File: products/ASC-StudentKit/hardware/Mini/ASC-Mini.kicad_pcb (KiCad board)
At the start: 2 copper layers, 97.4 x 47 mm, 92 parts, among them J1 12V IN, J10 OUT2, J2 USB-C, J3 PROG, J4 S1, J5 S2, J6 S3, J7 S4, J8 I2C-1 (Grove), J9 OUT1, K1 HF46F/005-HS1, K2 HF46F/005-HS1, Q1 AO3400A, Q2 AO3400A, Q3 AO3400A, SW1 RESET, SW2 PAIR / BOOT, U1 ESP32-S3-MINI-1-N8, U2 TPS54202DDC, U3 USBLC6-2SC6, U4 AP7361C-33E, U5 DS3231MZ+

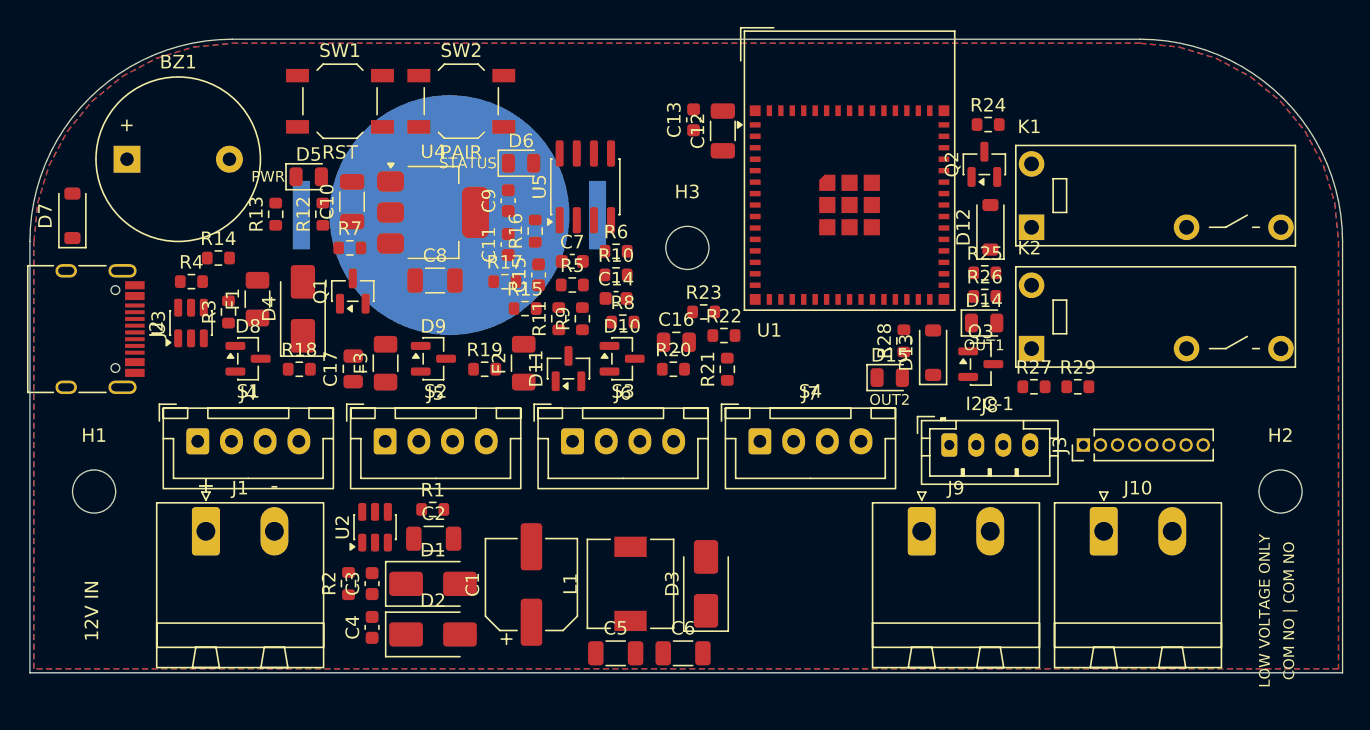
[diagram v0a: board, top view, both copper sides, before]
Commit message: Mini PCB: first Freerouting pass (partial: 19 connections open)
Freerouting 2.5.0, 18 passes, 0 violations: 1236 track segments and 112
vias. Still open: 44 GND connections (for the pours) and 14 on VIN,
VBUS_F, +3V3, +5V, EN, LED, LED_STATUS_A, RTC_INT and VIN_SENSE. The
placement gets loosened next.

Co-Authored-By: Claude Opus 5.5 <noreply@anthropic.com>
Claude-Session: https://claude.ai/code/session_0137TCDSR58nWZn1byy7MgSb
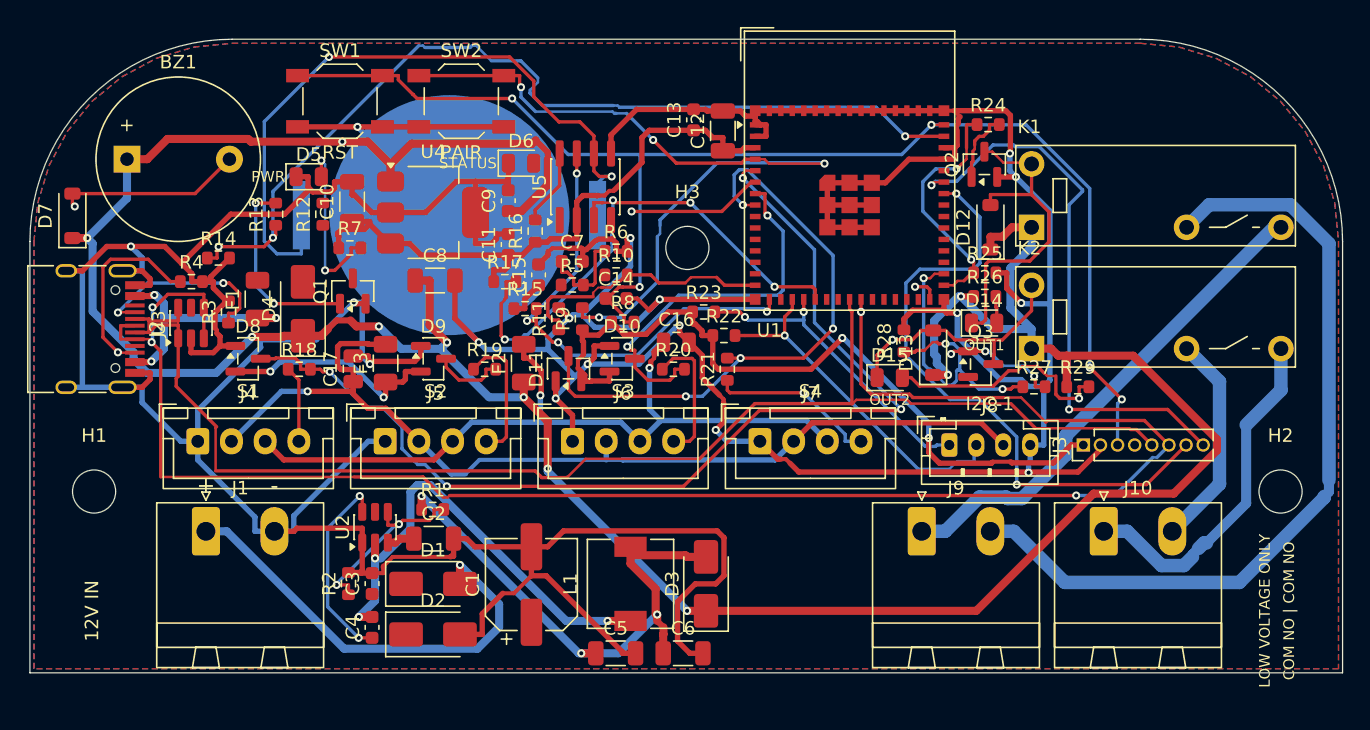
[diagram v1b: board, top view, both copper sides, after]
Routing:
- net GND: track 0.00 -> 492.9 mm, vias 0 -> 17
- net +5V: track 0.00 -> 215.9 mm, vias 0 -> 10
- net /USB_DP: track 0.00 -> 132.9 mm, vias 0 -> 4
- net +3V3: track 0.00 -> 121.4 mm, vias 0 -> 4
- net /USB_DN: track 0.00 -> 102.1 mm
- net /EN: track 0.00 -> 101.0 mm, vias 0 -> 5
- net /S1: track 0.00 -> 78.4 mm, vias 0 -> 4
- net /+3V3_PORT: track 0.00 -> 73.1 mm, vias 0 -> 1
- net /BUZZER: track 0.00 -> 69.0 mm, vias 0 -> 3
- net /OUT1_NO: track 0.00 -> 60.4 mm
- net /PAIR: track 0.00 -> 59.9 mm, vias 0 -> 4
- net /+5V_PORT: track 0.00 -> 58.5 mm, vias 0 -> 2
- net /VBAT_RTC: track 0.00 -> 52.1 mm, vias 0 -> 2
- net /TXD0: track 0.00 -> 46.3 mm, vias 0 -> 2
- net /S4: track 0.00 -> 44.4 mm, vias 0 -> 4
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
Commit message: Mini PCB: GND left to the pours, routing fixes
route.py leaves GND out of the autorouter: after import, each front SMD
GND pad gets a short track to its own via into the back pour, and a 4 mm
grid of stitching vias ties the two pours together. Every via and track
is checked for clearance against all other copper, the board edge, the
screw bosses and the antenna keep-out. Second run: 2 nets left open
(from 19). Clearance rule 0.19 mm (the USB-C footprint's own pad gaps
are exactly 0.2 mm).

Placement: R5 (VIN sense top) sits by the buck so VIN stays local; the
buzzer gate parts sit on Q1's gate; LED labels go under their LEDs. U3's
VBUS reference pin moves to VBUS (before the fuse).

Board in this commit is unrouted; the next run's result follows.

Co-Authored-By: Claude Opus 5.5 <noreply@anthropic.com>
Claude-Session: https://claude.ai/code/session_0137TCDSR58nWZn1byy7MgSb
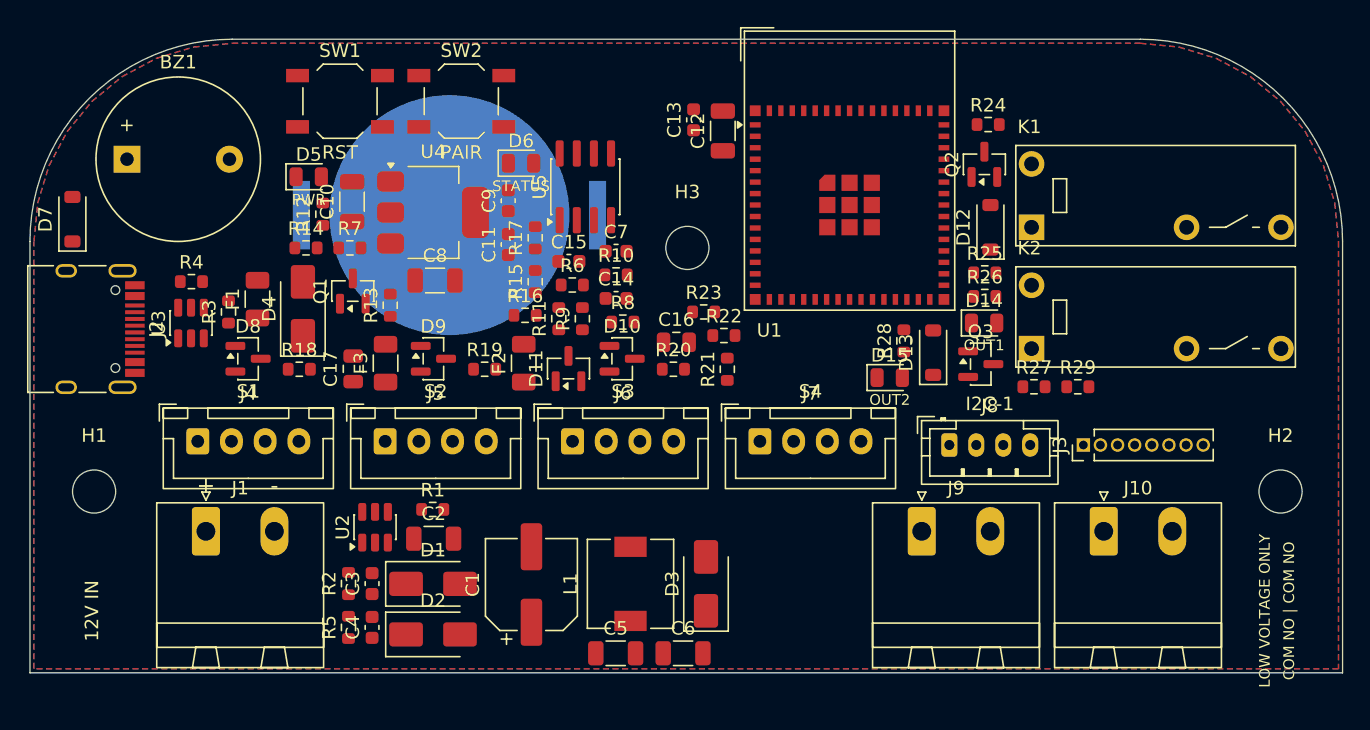
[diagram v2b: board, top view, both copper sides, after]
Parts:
- moved R5 30.3 mm to (123.6, 103.6), turned to 90 degrees
- moved R13 10.9 mm to (126.7, 79.7)
- moved R14 6.54 mm to (120.5, 75.5)
- moved R16 6.29 mm to (136.7, 80.5), turned to 0 degrees
- moved R6 4.10 mm to (140.2, 78.2)
- moved R17 3.95 mm to (137.5, 74.7), turned to 90 degrees
- moved C7 3.34 mm to (143.5, 75.7)
- moved C15 2.46 mm to (140.0, 76.5), turned to 0 degrees
- moved R15 2.14 mm to (137.5, 78.0), turned to 90 degrees
- moved D7 0.25 mm to (103.2, 73.3)
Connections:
- U3 pad 5: /VBUS_F -> /VBUS
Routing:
- net GND: track 492.9 -> 0.00 mm, vias 17 -> 0
- net +5V: track 215.9 -> 0.00 mm, vias 10 -> 0
- net /USB_DP: track 132.9 -> 0.00 mm, vias 4 -> 0
- net +3V3: track 121.4 -> 0.00 mm, vias 4 -> 0
- net /USB_DN: track 102.1 -> 0.00 mm
- net /EN: track 101.0 -> 0.00 mm, vias 5 -> 0
- net /S1: track 78.4 -> 0.00 mm, vias 4 -> 0
- net /+3V3_PORT: track 73.1 -> 0.00 mm, vias 1 -> 0
- net /BUZZER: track 69.0 -> 0.00 mm, vias 3 -> 0
- net /OUT1_NO: track 60.4 -> 0.00 mm
- net /PAIR: track 59.9 -> 0.00 mm, vias 4 -> 0
- net /+5V_PORT: track 58.5 -> 0.00 mm, vias 2 -> 0
- net /VBAT_RTC: track 52.1 -> 0.00 mm, vias 2 -> 0
- net /TXD0: track 46.3 -> 0.00 mm, vias 2 -> 0
- net /S4: track 44.4 -> 0.00 mm, vias 4 -> 0
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
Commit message: Mini PCB: all signals routed; pour check; GND routing stage
Variant b of three (power tracks 0.45 mm, supply 0.3 mm) routed every
signal connection (Freerouting 2.5.0, then its optimizer); its widths are
now the defaults. GND: pad vias, a 4 mm stitching grid, and island vias
from check_pour.py --fix.

tools/check_pour.py approximates KiCad's zone fill (0.1 mm raster, zone
clearance + half the minimum width) and checks every GND pad and via
lands in one connected GND. It still finds 16 pieces, where tracks on
both layers fence the pour in, so route.py gains a second stage
(ROUTE_STAGE=gnd): GND alone, routed as tracks around the protected
signal tracks.

Co-Authored-By: Claude Opus 5.5 <noreply@anthropic.com>
Claude-Session: https://claude.ai/code/session_0137TCDSR58nWZn1byy7MgSb
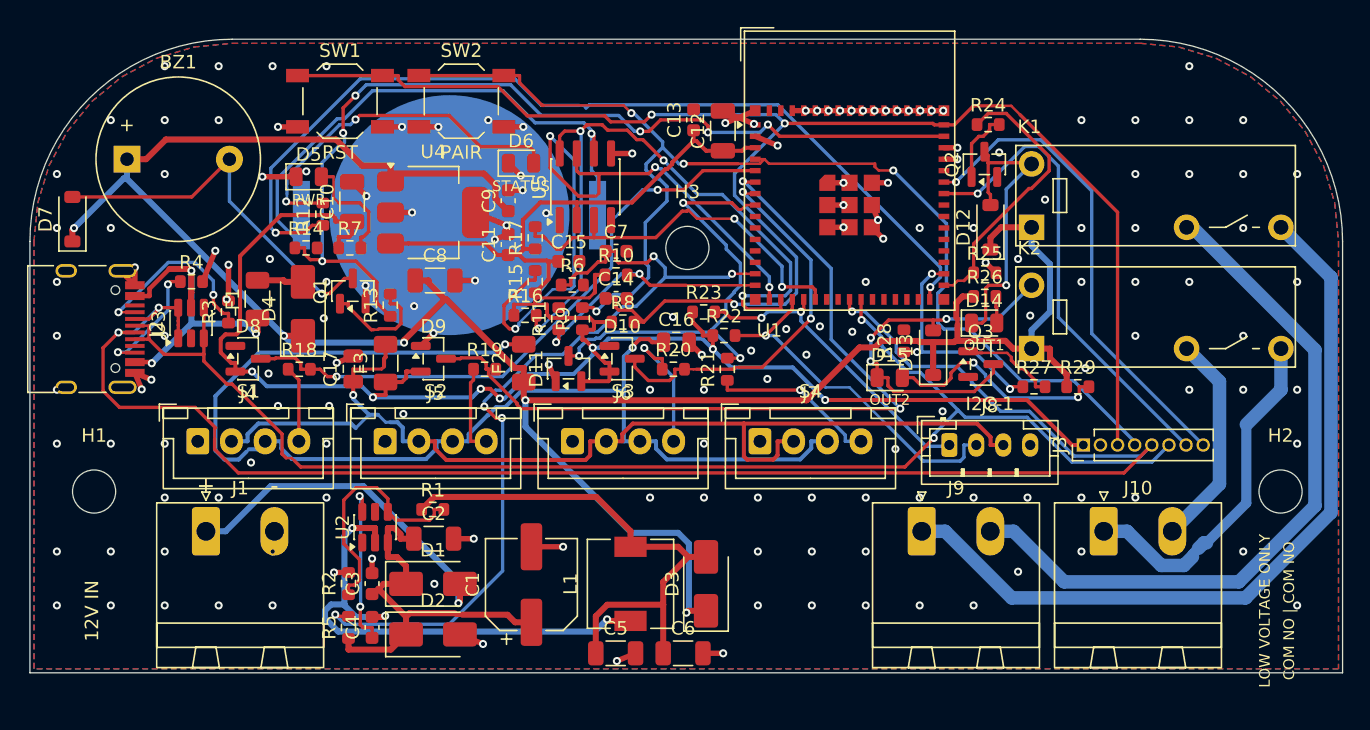
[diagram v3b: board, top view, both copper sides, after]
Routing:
- net +5V: track 0.00 -> 175.2 mm, vias 0 -> 5
- net +3V3: track 0.00 -> 168.3 mm, vias 0 -> 7
- net /USB_DN: track 0.00 -> 126.3 mm, vias 0 -> 3
- net /EN: track 0.00 -> 117.2 mm, vias 0 -> 3
- net /USB_DP: track 0.00 -> 103.2 mm, vias 0 -> 2
- net /+5V_PORT: track 0.00 -> 90.0 mm, vias 0 -> 2
- net /PAIR: track 0.00 -> 89.3 mm, vias 0 -> 4
- net /+3V3_PORT: track 0.00 -> 79.4 mm, vias 0 -> 1
- net GND: track 0.00 -> 78.4 mm, vias 0 -> 168
- net /BUZZER: track 0.00 -> 70.9 mm, vias 0 -> 6
- net /LED: track 0.00 -> 69.8 mm, vias 0 -> 2
- net /VIN_SENSE: track 0.00 -> 64.3 mm, vias 0 -> 5
- net /S2: track 0.00 -> 59.1 mm, vias 0 -> 2
- net /OUT1_COM: track 0.00 -> 57.7 mm
- net /I2C_INT_SDA: track 0.00 -> 53.1 mm, vias 0 -> 4
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
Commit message: Mini PCB: GND routing stage result (21 GND connections still open)
ROUTE_STAGE=gnd routed GND as tracks around the protected signals: 241
segments and 15 vias, 21 connections open; with the pours and 97
stitching vias, check_pour.py still finds 19 separate GND pieces. Two
layers at this density don't give a reliable GND.

Co-Authored-By: Claude Opus 5.5 <noreply@anthropic.com>
Claude-Session: https://claude.ai/code/session_0137TCDSR58nWZn1byy7MgSb
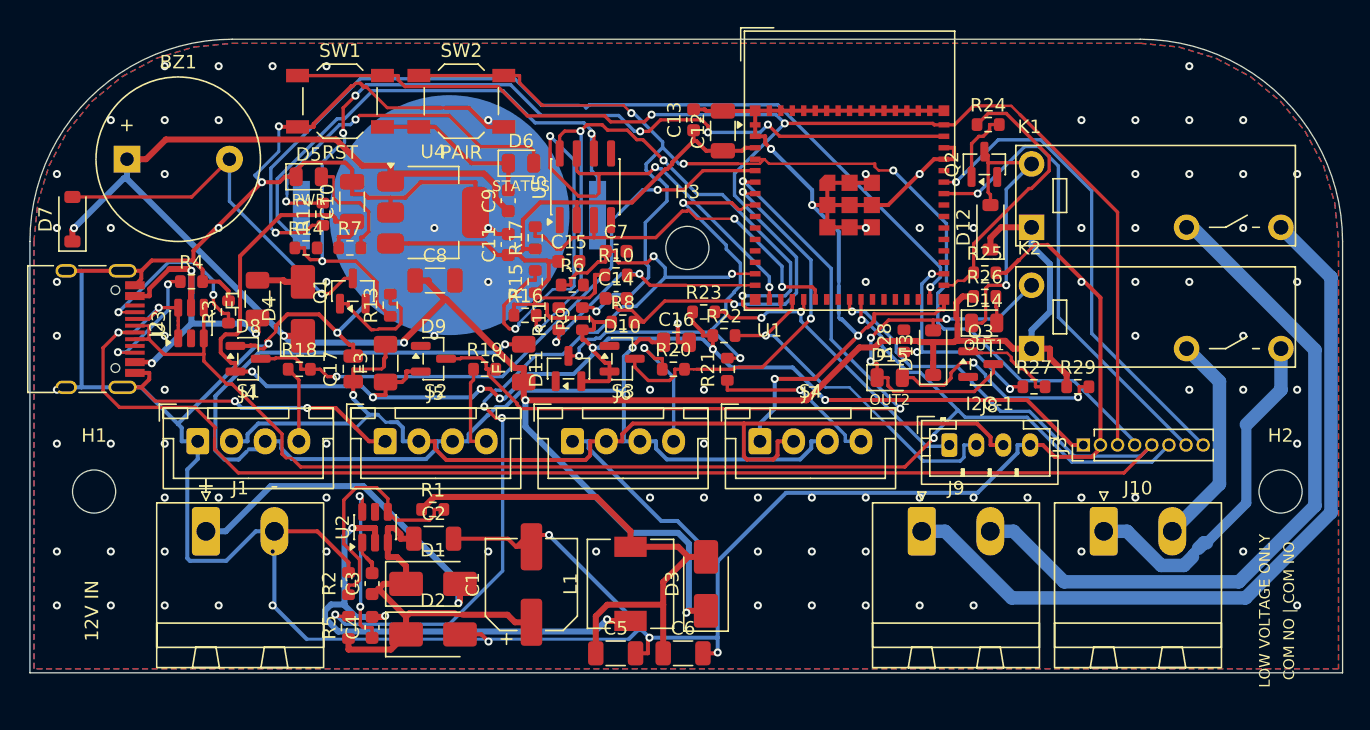
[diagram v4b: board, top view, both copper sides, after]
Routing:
- net GND: track 78.4 -> 417.6 mm, vias 168 -> 112

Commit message: Mini: 0402 passives, test header as pogo pads under the module
Staying on two layers frees routing room: the small resistors and
capacitors go from 0603 to 0402, and J3 (the tester's 8 pins) becomes an
SMD pad row on the back under the ESP32 module, not fitted (DNP), next
to the pins it serves instead of across the board. route.py gains
ROUTE_STAGE=all (GND routed with everything else). Board unrouted in
this commit; routing variants are running.

Co-Authored-By: Claude Opus 5.5 <noreply@anthropic.com>
Claude-Session: https://claude.ai/code/session_0137TCDSR58nWZn1byy7MgSb
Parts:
- C11, C13, C14, C15, C3, C4, C7, C9: footprint Capacitor_SMD:C_0603_1608Metric -> Capacitor_SMD:C_0402_1005Metric
- J3: value PROG -> PROG (pogo pads); footprint Connector_PinHeader_1.27mm:PinHeader_1x08_P1.27mm_Vertical -> Connector_PinHeader_1.27mm:PinHeader_1x08_P1.27mm_Vertical_SMD_Pin1Left; moved to B.Cu
- R1, R10, R11, R12, R13, R14, R15, R16, R17, R18, R19, R2, R20, R21, R22, R23, R24, R25, R26, R27, R28, R29, R3, R4, R5, R6, R7, R8, R9: footprint Resistor_SMD:R_0603_1608Metric -> Resistor_SMD:R_0402_1005Metric
- moved J3 26.8 mm to (156.8, 73.8), turned to 0 degrees
- moved D7 23.7 mm to (126.2, 79.1)
- moved R26 13.8 mm to (171.3, 65.3)
- moved D6 13.4 mm to (123.4, 72.5)
- moved R5 12.2 mm to (132.3, 95.1), turned to 0 degrees
- moved C10 12.0 mm to (135.9, 72.0)
- moved R25 11.4 mm to (169.6, 66.0), turned to 90 degrees
- moved C11 10.5 mm to (127.4, 68.5), turned to 0 degrees
- moved R28 9.16 mm to (173.4, 85.5), turned to 0 degrees
- moved C9 6.80 mm to (129.7, 68.5), turned to 0 degrees
- moved R14 5.85 mm to (124.0, 80.2), turned to 90 degrees
- moved C7 5.83 mm to (147.0, 80.4), turned to 90 degrees
- moved R7 5.39 mm to (124.7, 70.2), turned to 90 degrees
- moved R9 4.74 mm to (145.7, 80.7)
- moved R13 4.55 mm to (122.2, 79.7), turned to 0 degrees
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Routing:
- net GND: track 417.6 -> 0.00 mm, vias 112 -> 0
- net +5V: track 175.2 -> 0.00 mm, vias 5 -> 0
- net +3V3: track 168.3 -> 0.00 mm, vias 7 -> 0
- net /USB_DN: track 126.3 -> 0.00 mm, vias 3 -> 0
- net /EN: track 117.2 -> 0.00 mm, vias 3 -> 0
- net /USB_DP: track 103.2 -> 0.00 mm, vias 2 -> 0
- net /+5V_PORT: track 90.0 -> 0.00 mm, vias 2 -> 0
- net /PAIR: track 89.3 -> 0.00 mm, vias 4 -> 0
- net /+3V3_PORT: track 79.4 -> 0.00 mm, vias 1 -> 0
- net /BUZZER: track 70.9 -> 0.00 mm, vias 6 -> 0
- net /LED: track 69.8 -> 0.00 mm, vias 2 -> 0
- net /VIN_SENSE: track 64.3 -> 0.00 mm, vias 5 -> 0
- net /S2: track 59.1 -> 0.00 mm, vias 2 -> 0
- net /OUT1_COM: track 57.7 -> 0.00 mm
- net /I2C_INT_SDA: track 53.1 -> 0.00 mm, vias 4 -> 0
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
